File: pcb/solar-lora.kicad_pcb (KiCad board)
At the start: 2 copper layers, 60 x 60 mm, 49 parts, among them IC1 ATMEGA328P-A, P1 panel, P2 lipo, P3 therm, P4 CONN_01X16, P5 BNC, Q1 Q_NMOS_GSD, SW1 SW_PUSH, U1 mcp73871, U2 rfm9x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

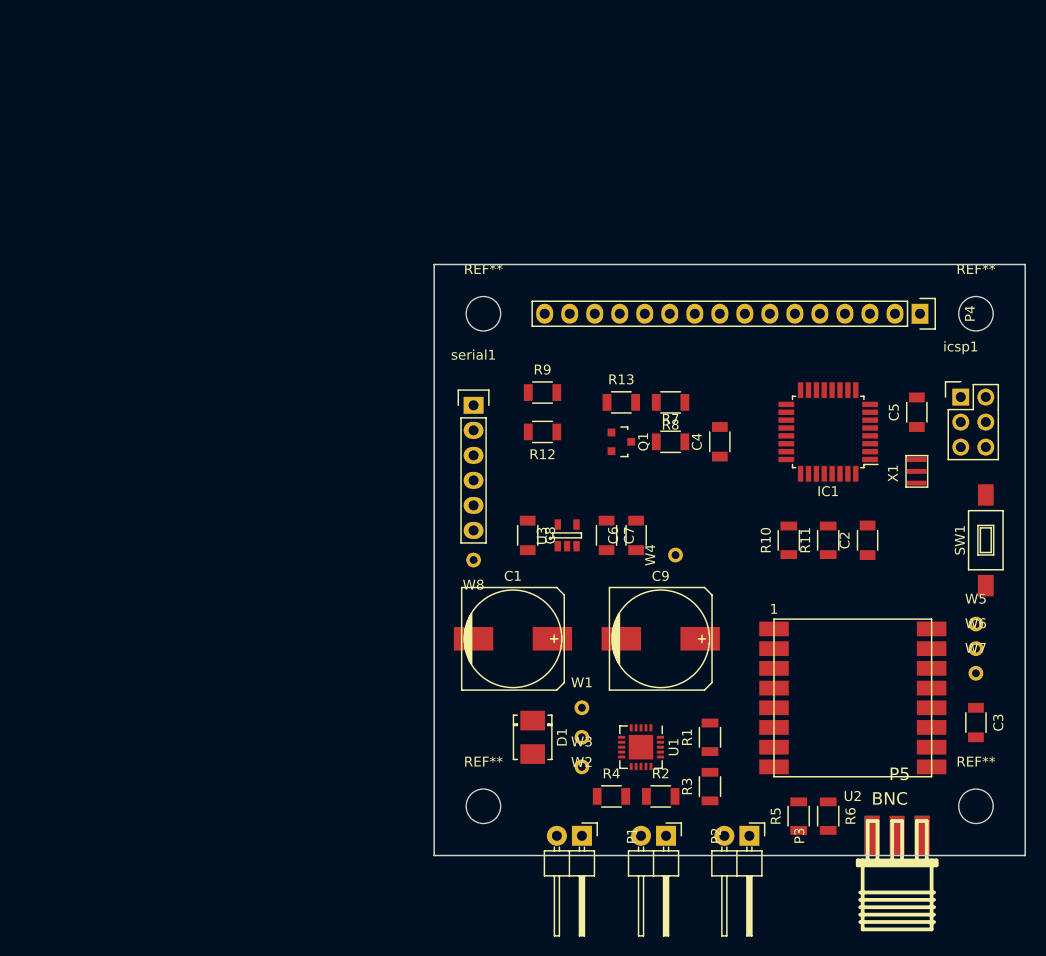
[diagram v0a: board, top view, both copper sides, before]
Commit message: schematic checked and first layout
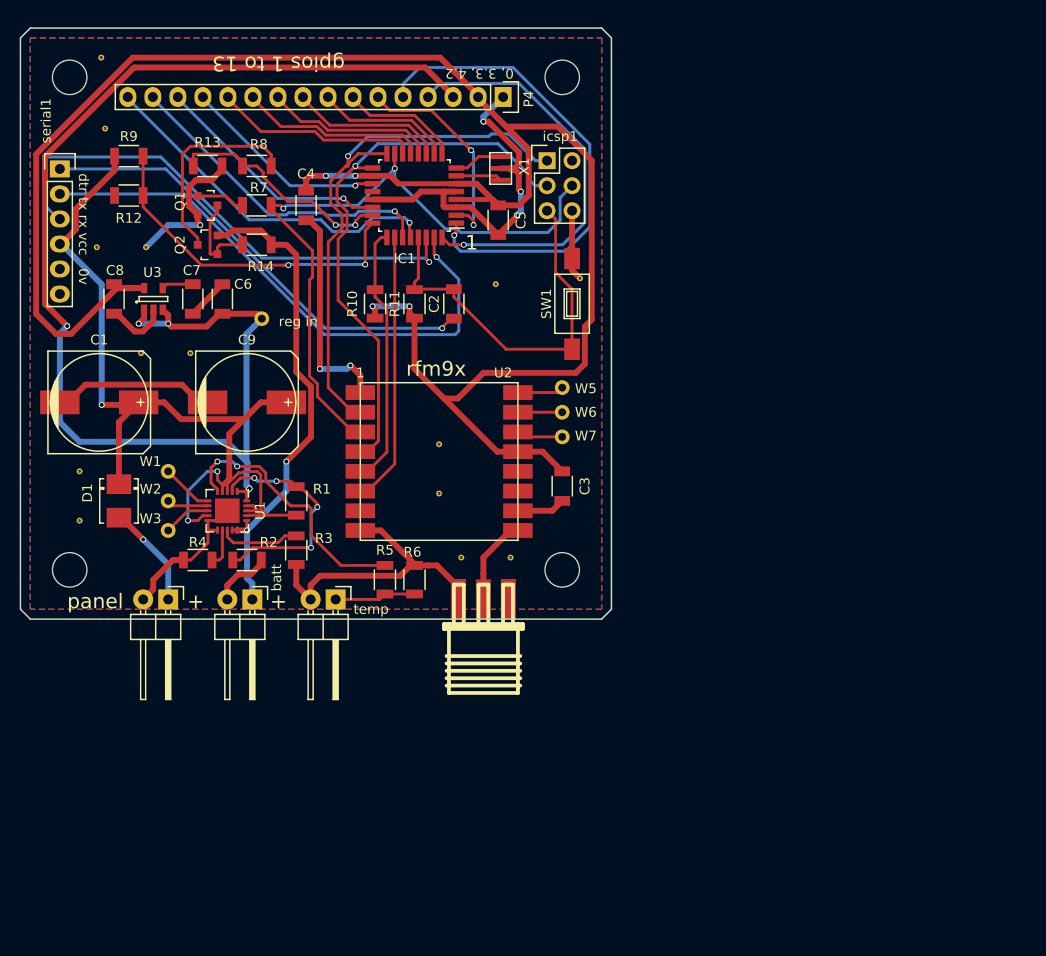
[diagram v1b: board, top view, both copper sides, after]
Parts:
- removed W8: TEST_1P, Measurement_Points:Measurement_Point_Round-TH_Small
- added Q2: Q_PMOS_GSD, Housings_SOT-23_SOT-143_TSOT-6:SOT-23, F.Cu at (152.0, 99.0)
- added R14: 10k, Resistors_SMD:R_1206, F.Cu at (157.0, 99.0)
- added REF**: via, fp:via, F.Cu at (141.6, 87.2)
- added REF**: via, fp:via, F.Cu at (189.8, 102.4)
- added REF**: via, fp:via, F.Cu at (182.8, 130.8)
- added REF**: via, fp:via, F.Cu at (177.8, 130.8)
- added REF**: via, fp:via, F.Cu at (145.2, 110.0)
- added REF**: via, fp:via, F.Cu at (181.2, 103.0)
- added REF**: via, fp:via, F.Cu at (145.8, 99.2)
- added REF**: via, fp:via, F.Cu at (140.8, 99.2)
- added REF**: via, fp:via, F.Cu at (141.2, 80.0)
- added REF**: via, fp:via, F.Cu at (139.0, 127.0)
- added REF**: via, fp:via, F.Cu at (175.5, 124.2)
- added REF**: via, fp:via, F.Cu at (139.0, 122.0)
- added REF**: via, fp:via, F.Cu at (175.5, 119.2)
- added REF**: via, fp:via, F.Cu at (150.2, 110.0)
- Q1: value Q_NMOS_GSD -> BC849; footprint TO_SOT_Packages_SMD:SOT-23 -> Housings_SOT-23_SOT-143_TSOT-6:SOT-23
- reg in: renamed from W4
- moved X1 52.3 mm to (181.8, 91.2), turned to 90 degrees
- moved C1 48.4 mm to (141.0, 115.0)
- moved C2 48.4 mm to (177.0, 105.0)
- moved C3 48.4 mm to (188.0, 123.5)
- moved C4 48.4 mm to (162.0, 95.0)
- moved C6 48.4 mm to (153.5, 104.5)
- moved C7 48.4 mm to (150.5, 104.5)
- moved C8 48.4 mm to (142.5, 104.5)
- moved C9 48.4 mm to (156.0, 115.0)
- moved D1 48.4 mm to (143.0, 125.0)
- moved IC1 48.4 mm to (173.0, 94.0)
- moved P1 48.4 mm to (148.0, 135.0)
- moved P2 48.4 mm to (156.5, 135.0)
- moved P3 48.4 mm to (165.0, 135.0)
- moved P5 48.4 mm to (180.0, 135.0)
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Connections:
- IC1 pad 22: Net-(IC1-Pad22) -> gpio11
- IC1 pad 26: gpio11 -> rfm-reset
- P1 pad 1: Earth -> Net-(D1-Pad2)
- P1 pad 2: Net-(D1-Pad2) -> Earth
- Q1 pad 1: divider -> Net-(Q1-Pad1)
- R13 pad 2: Net-(Q1-Pad3) -> Earth
- R7 pad 1: divider -> Net-(Q1-Pad1)
- R7 pad 2: Earth -> divider
- R8 pad 1: batt -> Net-(Q2-Pad3)
- U2 pad 6: (no net) -> rfm-reset
- serial1 pad 4: reg_in -> VCC
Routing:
- net +3V3: track 0.00 -> 203.7 mm, vias 0 -> 4
- net Earth: track 0.00 -> 164.9 mm, vias 0 -> 6
- net reg_in: track 0.00 -> 132.5 mm, vias 0 -> 5
- net VCC: track 0.00 -> 94.7 mm, vias 0 -> 3
- net divider: track 0.00 -> 67.9 mm, vias 0 -> 2
- net sck: track 0.00 -> 59.0 mm, vias 0 -> 1
- net tx: track 0.00 -> 57.1 mm, vias 0 -> 1
- net miso: track 0.00 -> 56.5 mm, vias 0 -> 1
- net rx: track 0.00 -> 52.8 mm, vias 0 -> 1
- net batt: track 0.00 -> 50.5 mm, vias 0 -> 2
- net gpio2: track 0.00 -> 49.9 mm, vias 0 -> 1
- net Net-(C2-Pad1): track 0.00 -> 47.2 mm, vias 0 -> 1
- net gpio1: track 0.00 -> 42.5 mm, vias 0 -> 1
- net reset: track 0.00 -> 39.6 mm
- net gpio13: track 0.00 -> 36.7 mm, vias 0 -> 1
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- added copper zone on B.Cu, net Earth
- added copper zone on F.Cu, net Earth
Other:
- outline, holes or cut-outs redrawn
- net class Default: clearance 0.2 -> 0.15; trace_width 0.25 -> 0.3
- net class power: trace_width 0.4 -> 0.6
- rule trace_clearance: 0.2 -> 0.15
- board text added: "+"
- board text added: "0, 3.3, 4.2"
- board text added: "1"
- board text added: "Matt Venn 2017 Solar Lora Node Open Hardware"
- board text added: "batt"
- board text added: "dtr tx rx vcc 0v"
- board text added: "gpios 1 to 13"
- board text added: "panel"
- board text added: "rfm9x"
- board text added: "temp"

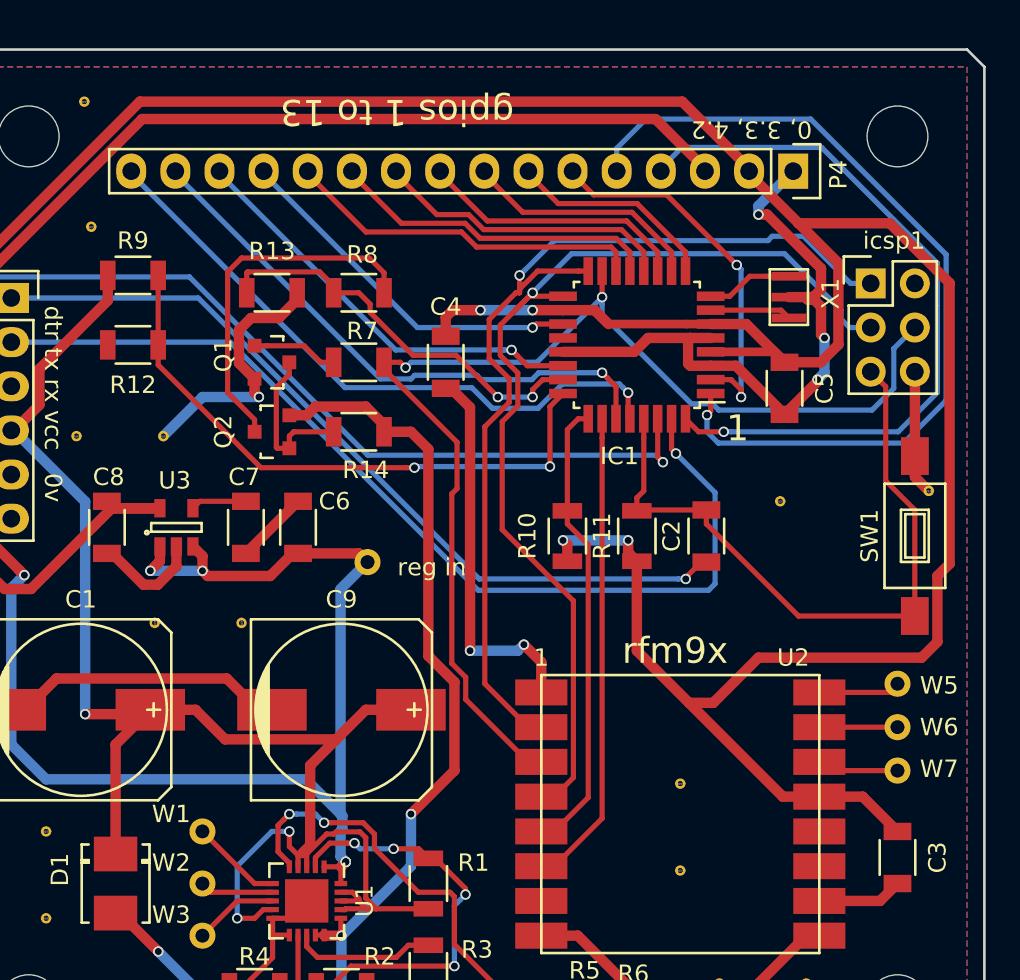
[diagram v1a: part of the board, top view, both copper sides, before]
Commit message: sent to fab and resistor calcs for charger
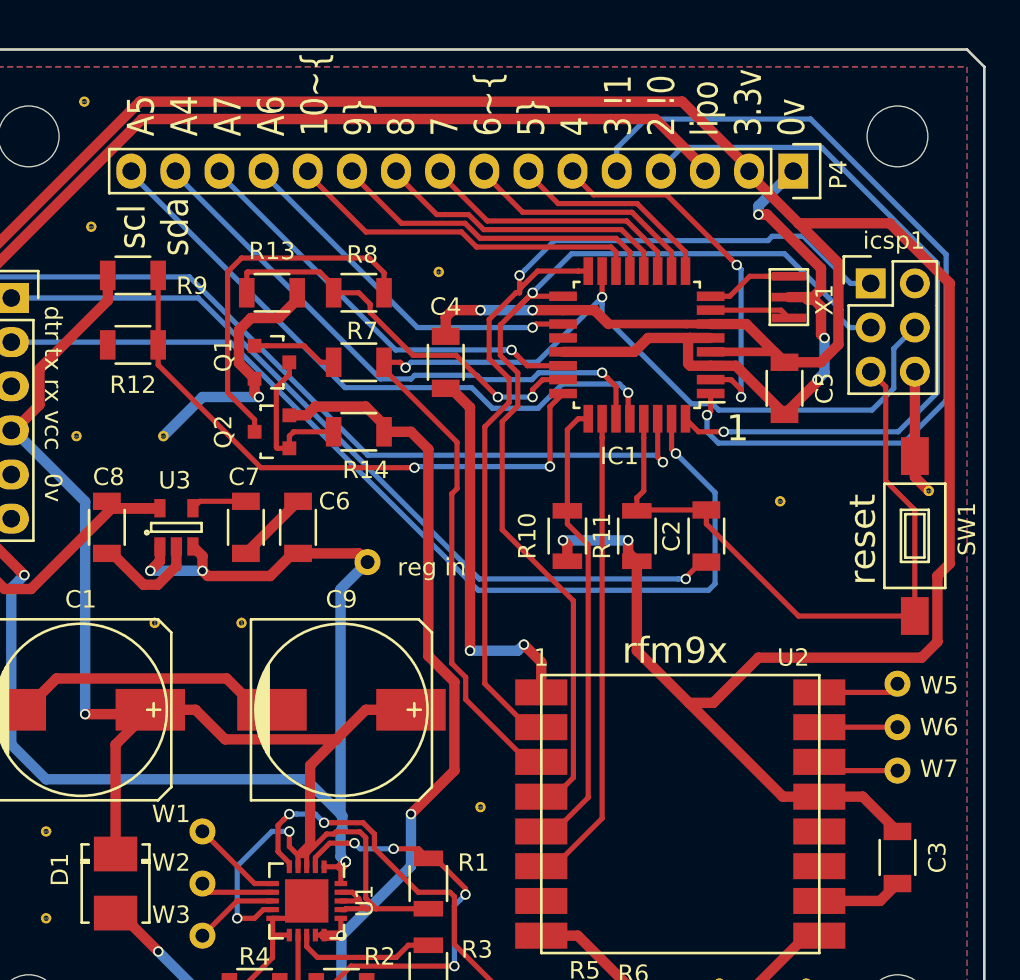
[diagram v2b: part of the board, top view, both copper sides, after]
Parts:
- moved REF** 37.1 mm to (161.6, 89.8)
- moved REF** 11.6 mm to (164.0, 120.6)
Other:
- board text added: "A5 A4 A7 A6 10~ 9~ 8 7 6~ 5~ 4 3 !1 2 !0 lipo 3.3v 0v"
- board text added: "reset"
- board text added: "scl sda"
- board text removed: "0, 3.3, 4.2"
- board text removed: "gpios 1 to 13"
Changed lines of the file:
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@@
     (links 139)
     (no_connects 0)
-    (area 171.490476 100.52412 238.509524 169.875001)
+    (area 127.657143 69.625 206.542858 145.875001)
     (thickness 1.6)
-    (drawings 19)
+    (drawings 24)
     (tracks 637)
     (zones 0)
@@
     (visible_elements FFFFFF7F)
     (pcbplotparams
-      (layerselection 0x00030_80000001)
+      (layerselection 0x010f0_80000001)
       (usegerberextensions false)
       (excludeedgelayer true)
@@
       (outputformat 1)
       (mirror false)
-      (drillshape 1)
+      (drillshape 0)
       (scaleselection 1)
-      (outputdirectory ""))
+      (outputdirectory fab/))
   )
   (net 0 "")
@@
   )
   (module fp:via (layer F.Cu)
-    (at 175.5 124.25)
+    (at 161.6 89.8)
     (fp_text reference REF** (at 0.075 0.025) (layer F.SilkS)
       (effects (font (size 0.127 0.127) (thickness 0.03175)))
@@
   )
   (module fp:via (layer F.Cu)
-    (at 175.5 119.25)
+    (at 164 120.6)
     (fp_text reference REF** (at 0.075 0.025) (layer F.SilkS)
       (effects (font (size 0.127 0.127) (thickness 0.03175)))
@@
     (tags "resistor 1206")
     (attr smd)
-    (fp_text reference R9 (at 0 -2) (layer F.SilkS)
+    (fp_text reference R9 (at 3.4 0.6) (layer F.SilkS)
       (effects (font (size 1 1) (thickness 0.15)))
     )
@@
     (tags "SPST button tactile switch")
     (attr smd)
-    (fp_text reference SW1 (at 0.01011 -2.60022 90) (layer F.SilkS)
+    (fp_text reference SW1 (at 0.4 3 90) (layer F.SilkS)
       (effects (font (size 1 1) (thickness 0.15)))
     )
@@
   (module fp:cstce-v (layer F.Cu)
     (at 181.75 91.25 90)
-    (fp_text reference X1 (at 0.2 2.4 90) (layer F.SilkS)
+    (fp_text reference X1 (at -0.15 2.05 90) (layer F.SilkS)
       (effects (font (size 1 1) (thickness 0.15)))
     )
@@
       (net 1 Earth) (zone_connect 2))
   )
+  (dimension 60 (width 0.3) (layer F.SilkS)
+    (gr_text "60.000 mm" (at 123.65 107 270) (layer F.SilkS)
+      (effects (font (size 1.5 1.5) (thickness 0.3)))
+    )
+    (feature1 (pts (xy 133 137) (xy 122.3 137)))
+    (feature2 (pts (xy 133 77) (xy 122.3 77)))
+    (crossbar (pts (xy 125 77) (xy 125 137)))
+    (arrow1a (pts (xy 125 137) (xy 124.413579 135.873496)))
+    (arrow1b (pts (xy 125 137) (xy 125.586421 135.873496)))
+    (arrow2a (pts (xy 125 77) (xy 124.413579 78.126504)))
+    (arrow2b (pts (xy 125 77) (xy 125.586421 78.126504)))
+  )
+  (dimension 60 (width 0.3) (layer F.SilkS)
+    (gr_text "60.000 mm" (at 163 63.65) (layer F.SilkS)
+      (effects (font (size 1.5 1.5) (thickness 0.3)))
+    )
+    (feature1 (pts (xy 193 77) (xy 193 62.3)))
+    (feature2 (pts (xy 133 77) (xy 133 62.3)))
+    (crossbar (pts (xy 133 65) (xy 193 65)))
+    (arrow1a (pts (xy 193 65) (xy 191.873496 65.586421)))
+    (arrow1b (pts (xy 193 65) (xy 191.873496 64.413579)))
+    (arrow2a (pts (xy 133 65) (xy 134.126504 65.586421)))
+    (arrow2b (pts (xy 133 65) (xy 134.126504 64.413579)))
+  )
+  (dimension 50 (width 0.3) (layer F.SilkS)
+    (gr_text "50.000 mm" (at 201.35 107 270) (layer F.SilkS)
+      (effects (font (size 1.5 1.5) (thickness 0.3)))
+    )
+    (feature1 (pts (xy 188 132) (xy 202.7 132)))
+    (feature2 (pts (xy 188 82) (xy 202.7 82)))
+    (crossbar (pts (xy 200 82) (xy 200 132)))
+    (arrow1a (pts (xy 200 132) (xy 199.413579 130.873496)))
+    (arrow1b (pts (xy 200 132) (xy 200.586421 130.873496)))
+    (arrow2a (pts (xy 200 82) (xy 199.413579 83.126504)))
+    (arrow2b (pts (xy 200 82) (xy 200.586421 83.126504)))
+  )
+  (dimension 50 (width 0.3) (layer F.SilkS)
+    (gr_text "50.000 mm" (at 163 69.65) (layer F.SilkS)
+      (effects (font (size 1.5 1.5) (thickness 0.3)))
+    )
+    (feature1 (pts (xy 188 82) (xy 188 68.3)))
+    (feature2 (pts (xy 138 82) (xy 138 68.3)))
+    (crossbar (pts (xy 138 71) (xy 188 71)))
+    (arrow1a (pts (xy 188 71) (xy 186.873496 71.586421)))
+    (arrow1b (pts (xy 188 71) (xy 186.873496 70.413579)))
+    (arrow2a (pts (xy 138 71) (xy 139.126504 71.586421)))
+    (arrow2b (pts (xy 138 71) (xy 139.126504 70.413579)))
+  )
+  (gr_text "scl\nsda" (at 145.2 87.2 90) (layer F.SilkS)
+    (effects (font (size 1.55 1.4) (thickness 0.2)))
+  )
+  (gr_text "A5\nA4\nA7\nA6\n10~\n9~\n8\n7\n6~\n5~\n4\n3 !1\n2 !0\nlipo\n3.3v\n0v" (at 163.2 82 90) (layer F.SilkS)
+    (effects (font (size 1.55 1.3) (thickness 0.2)) (justify left))
+  )
+  (gr_text reset (at 186 105.2 90) (layer F.SilkS)
+    (effects (font (size 1.5 1.5) (thickness 0.3)))
+  )
   (gr_line (start 192 137) (end 193 136) (layer Edge.Cuts) (width 0.15))
   (gr_line (start 133 136) (end 134 137) (layer Edge.Cuts) (width 0.15))
@@
     (effects (font (size 1.5 1.5) (thickness 0.3)))
   )
-  (gr_text "0, 3.3, 4.2" (at 179.6 81.6 180) (layer F.SilkS)
-    (effects (font (size 1 1) (thickness 0.25)))
-  )
-  (gr_text "gpios 1 to 13" (at 159.2 80.6 180) (layer F.SilkS)
-    (effects (font (size 1.5 1.5) (thickness 0.3)))
-  )
